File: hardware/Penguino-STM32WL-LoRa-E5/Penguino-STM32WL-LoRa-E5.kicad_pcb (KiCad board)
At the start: 2 copper layers, 22.9 x 50.8 mm, 59 parts, among them J1 JST_PH, J2 USB_C_Receptacle_USB2.0, J3 Conn_ARM_JTAG_SWD_10, J4 U.FL/iPEX, J5 SMA-Edge-Mount, Q1 NCE3407A, SW1 RESET, SW2 USR_BTN, U1 MCP73831, U2 RT9078-33GJ5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

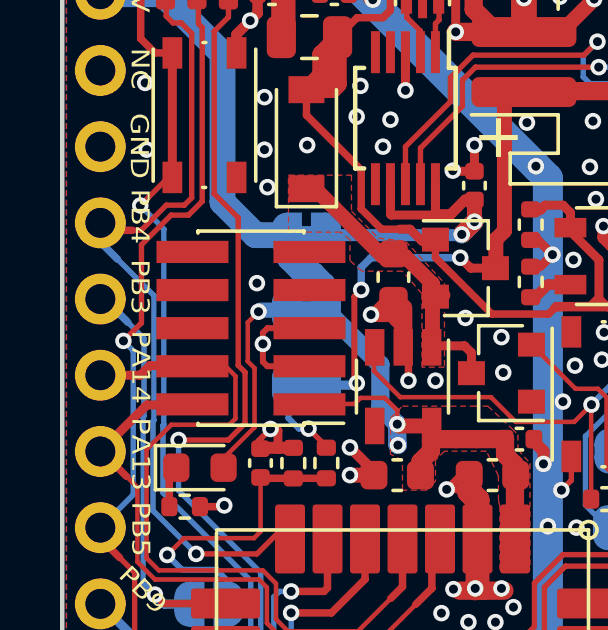
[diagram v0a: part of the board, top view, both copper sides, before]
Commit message: fix: NRST and USB Footprint
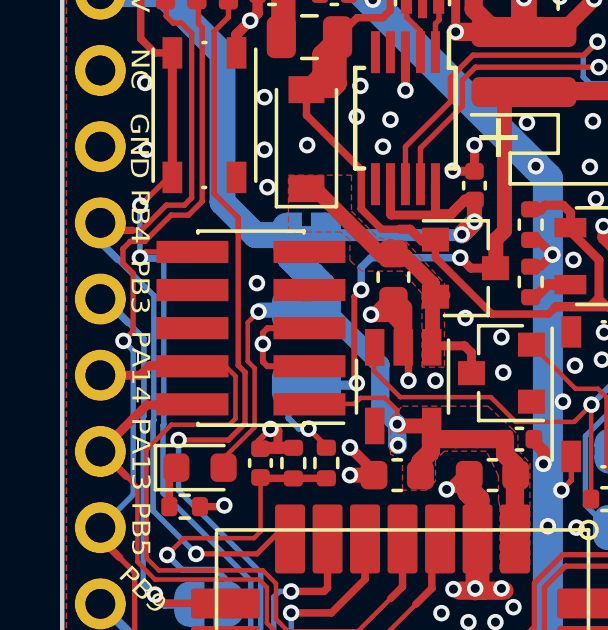
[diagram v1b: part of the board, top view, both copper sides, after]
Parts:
- removed G***: LOGO, Custom_Logos:Makertronika-1500
- R14: value 2M -> 1M
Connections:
- J3 pad 10: (no net) -> RST
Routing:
- net RST: track 40.0 -> 43.1 mm, vias 2 -> 3
- net PB5: track 29.6 -> 30.2 mm
